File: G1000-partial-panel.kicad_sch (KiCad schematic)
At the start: 3 parts

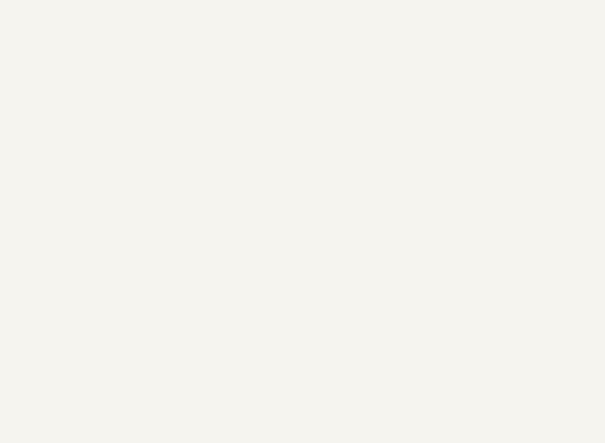
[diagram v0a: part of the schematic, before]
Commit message: Redo panel
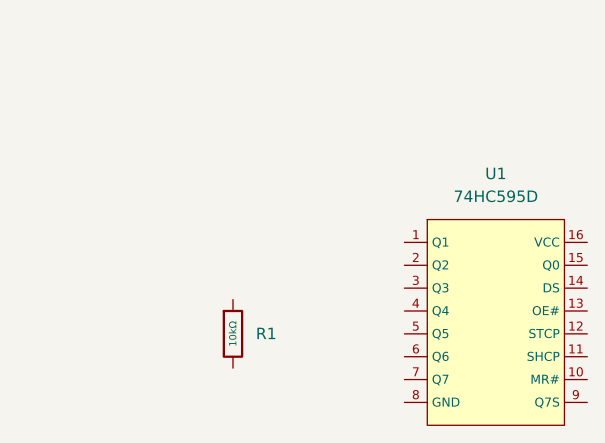
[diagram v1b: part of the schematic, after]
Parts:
- added R1: 10kΩ, PCM_JLCPCB:R_0402, symbol PCM_JLCPCB-Resistors:0402,10kΩ
- added U1: 74HC595D, PCM_JLCPCB:SOIC-16_L9.9-W3.9-P1.27-LS6.0-BL, symbol PCM_JLCPCB-ICs:Shift Register, 1 In, 8 Out, 74HC595D,118
